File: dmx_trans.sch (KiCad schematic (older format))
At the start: 56 parts, among them IC1 SP3485EP, J1 DB9, K1 CONN_3, K2 CONN_3, P1 CONN_2, P2 CONN_5X2, P3 LCD_CONN, SW1 RESET_BTN, SW2 PROG_BTN, U1 NCP1117ST33T3G, U2 STM32F100C6, U3 ST3232CD, X1 8MHz

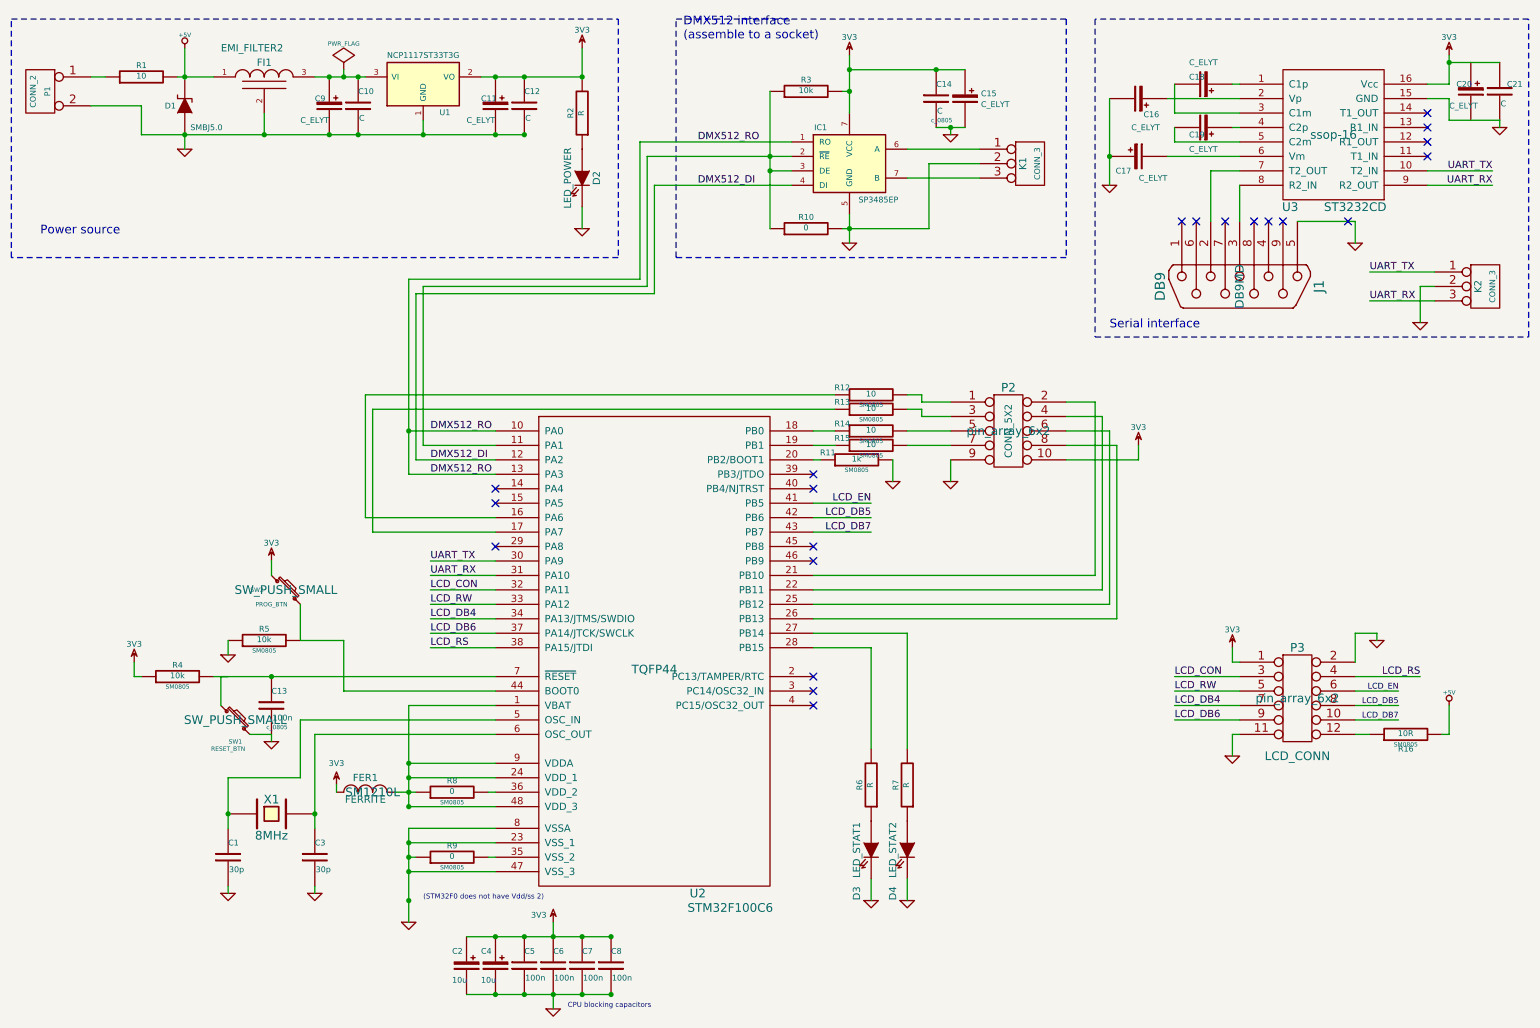
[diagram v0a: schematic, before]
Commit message: Schematics updated
- filled values
- filled title block
- connector fixes
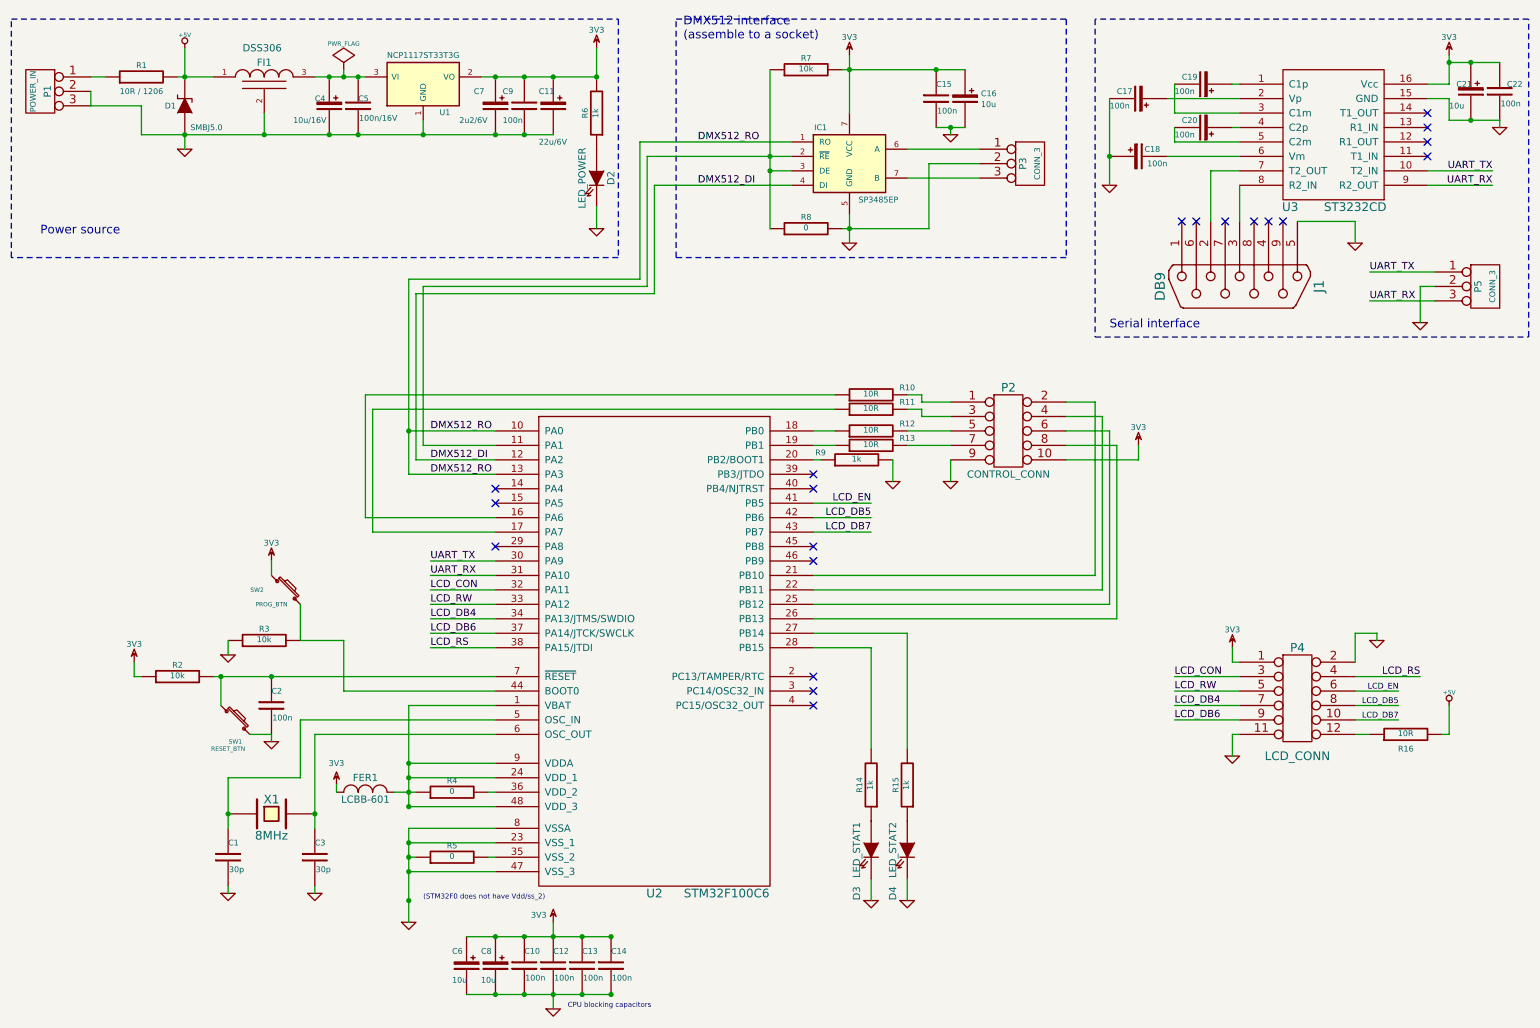
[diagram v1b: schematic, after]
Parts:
- removed P1: CONN_2, JACK_ALIM, symbol CONN_2
- added C11: 22u/6V, c_0805, symbol C_ELYT
- added P1: POWER_IN, PIN_ARRAY_3X1, symbol CONN_3
- C15: renamed from C14; value C -> 100n
- C16: renamed from C15; value C_ELYT -> 10u
- C17: renamed from C16; value C_ELYT -> 100n
- C18: renamed from C17; value C_ELYT -> 100n
- C19: renamed from C18; value C_ELYT -> 100n
- C20: renamed from C19; value C_ELYT -> 100n
- C21: renamed from C20; value C_ELYT -> 10u
- C22: renamed from C21; value C -> 100n
- C4: renamed from C9; value C_ELYT -> 10u/16V
- C5: renamed from C10; value C -> 100n/16V
- C7: renamed from C11; value C_ELYT -> 2u2/6V
- C9: renamed from C12; value C -> 100n
- FER1: value FERRITE -> LCBB-601
- FI1: value EMI_FILTER2 -> DSS306
- P2: value CONN_5X2 -> CONTROL_CONN
- R1: value 10 -> 10R / 1206
- R10: renamed from R12; value 10 -> 10R
- R11: renamed from R13; value 10 -> 10R
- R12: renamed from R14; value 10 -> 10R
- R13: renamed from R15; value 10 -> 10R
- R14: renamed from R6; value R -> 1k
- R15: renamed from R7; value R -> 1k
- R6: renamed from R2; value R -> 1k
- renumbered C5 to C10, C6 to C12, C7 to C13, C8 to C14, C13 to C2, C2 to C6, C4 to C8, K1 to P3, P3 to P4, K2 to P5, R4 to R2, R5 to R3, R8 to R4, R9 to R5, R3 to R7, R10 to R8, R11 to R9
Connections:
- net 3V3: now also C21.1, C11.1
- net GND: now also C21.2, C11.2, P1.2 (PM), P1.3 (P3)
- net at R1.1: now also P1.1 (P1)
- no-connect marks 21 -> 20
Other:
- note added: "(STM32F0 does not have Vdd/ss_2)"
- note removed: "(STM32F0 does not have Vdd/ss 2)"
- moved on the sheet: D2, R6, R7

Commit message: Start of routing
- footprints assigned
- initial part placement
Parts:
- C11, C4, C5, C6, C7, C8: footprint c_0805 -> c_tant_A
- C16, C21: footprint (none) -> c_tant_A
- C17, C18, C19, C20, C22: footprint (none) -> c_0805
- D1: footprint SM1206POL -> DO-214AA(SMB)
- FER1: footprint SM1210L -> SM0805
- FI1: footprint PIN_ARRAY_3X1 -> DSS6
- J1: footprint DB9MD -> DB9M_CI
- P1: footprint PIN_ARRAY_3X1 -> BARREL_JACK
- P2: footprint pin_array_6x2 -> PIN_ARRAY_5x2
- P3: value CONN_3 -> DMX512_CON; footprint PIN_ARRAY_3X1 -> PINHEAD1-3
- P5: value CONN_3 -> UART_CON
- R8: value 0 -> N/A
- SW1, SW2: footprint SW_PUSH_SMALL -> switch-tact-DTSM-3
- U2: footprint TQFP44 -> LQFP48
- U3: footprint ssop-16 -> SO16N
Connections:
- net +5V: now also C4.1, C5.1, FI1.3 (VO), U1.3 (VI); no longer D1.2 (K), FI1.1 (VI), R1.2
- new net: D1.2 (K), FI1.1 (VI), R1.2
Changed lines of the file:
@@
-EESchema Schematic File Version 2  date 18/05/2013 11:10:39
+EESchema Schematic File Version 2  date 18/05/2013 19:06:34
 LIBS:power
 LIBS:device
@@
 F 0 "D1" V 1850 1300 40  0000 C CNN
 F 1 "SMBJ5.0" V 1700 1050 40  0000 C CNN
-F 2 "SM1206POL" H 1850 1200 60  0001 C CNN
+F 2 "DO-214AA(SMB)" H 1850 1200 60  0001 C CNN
 F 3 "~" H 1850 1200 60  0000 C CNN
 	1    1850 1200
@@
 F 0 "FI1" H 2400 1100 50  0000 C CNN
 F 1 "DSS306" H 2250 1200 50  0000 L CNN
-F 2 "PIN_ARRAY_3X1" H 2400 1000 60  0001 C CNN
+F 2 "DSS6" H 2400 1000 60  0001 C CNN
 F 3 "~" H 2400 1000 60  0000 C CNN
 	1    2400 1000
@@
 F 0 "C5" H 3050 1250 40  0000 L CNN
 F 1 "100n/16V" H 3056 1115 40  0000 L CNN
-F 2 "c_0805" H 3088 1050 30  0001 C CNN
+F 2 "c_tant_A" H 3088 1050 30  0001 C CNN
 F 3 "~" H 3050 1200 60  0000 C CNN
 	1    3050 1200
@@
 F 0 "C4" H 2750 1250 40  0000 L CNN
 F 1 "10u/16V" H 2600 1100 40  0000 L CNN
-F 2 "c_0805" H 2888 1050 30  0001 C CNN
+F 2 "c_tant_A" H 2888 1050 30  0001 C CNN
 F 3 "~" H 2850 1200 60  0000 C CNN
 	1    2850 1200
@@
 F 0 "C7" H 3850 1300 40  0000 L CNN
 F 1 "2u2/6V" H 3750 1100 40  0000 L CNN
-F 2 "c_0805" H 4038 1050 30  0001 C CNN
+F 2 "c_tant_A" H 4038 1050 30  0001 C CNN
 F 3 "~" H 4000 1200 60  0000 C CNN
 	1    4000 1200
@@
 F 0 "C8" H 3900 7250 40  0000 L CNN
 F 1 "10u" H 3900 7050 40  0000 L CNN
-F 2 "c_0805" H 4038 7000 30  0001 C CNN
+F 2 "c_tant_A" H 4038 7000 30  0001 C CNN
 F 3 "~" H 4000 7150 60  0000 C CNN
 	1    4000 7150
@@
 F 0 "C6" H 3700 7250 40  0000 L CNN
 F 1 "10u" H 3700 7050 40  0000 L CNN
-F 2 "c_0805" H 3838 7000 30  0001 C CNN
+F 2 "c_tant_A" H 3838 7000 30  0001 C CNN
 F 3 "~" H 3800 7150 60  0000 C CNN
 	1    3800 7150
@@
 P 7700 1600
 F 0 "P3" V 7650 1600 50  0000 C CNN
-F 1 "CONN_3" V 7750 1600 40  0000 C CNN
-F 2 "PIN_ARRAY_3X1" H 7700 1600 60  0001 C CNN
+F 1 "DMX512_CON" H 7650 1400 40  0000 C CNN
+F 2 "PINHEAD1-3" H 7700 1600 60  0001 C CNN
 F 3 "" H 7700 1600 60  0000 C CNN
 	1    7700 1600
@@
 F 0 "SW1" H 2200 5300 30  0000 C CNN
 F 1 "RESET_BTN" H 2150 5250 30  0000 C CNN
-F 2 "SW_PUSH_SMALL" H 2200 5450 60  0001 C CNN
+F 2 "switch-tact-DTSM-3" H 2200 5450 60  0001 C CNN
 F 3 "~" H 2200 5450 60  0000 C CNN
 	1    2200 5450
@@
 F 0 "U2" H 5100 3550 60  0000 C CNN
 F 1 "STM32F100C6" H 5600 3550 60  0000 C CNN
-F 2 "TQFP44" H 5100 5100 60  0001 C CNN
+F 2 "LQFP48" H 5100 5100 60  0001 C CNN
 F 3 "" H 5100 5100 60  0000 C CNN
 	1    5100 5100
@@
 F 0 "SW2" H 2350 4550 30  0000 C CNN
 F 1 "PROG_BTN" H 2450 4450 30  0000 C CNN
-F 2 "SW_PUSH_SMALL" H 2550 4550 60  0001 C CNN
+F 2 "switch-tact-DTSM-3" H 2550 4550 60  0001 C CNN
 F 3 "~" H 2550 4550 60  0000 C CNN
 	1    2550 4550
@@
 P 10850 2450
 F 0 "P5" V 10800 2450 50  0000 C CNN
-F 1 "CONN_3" V 10900 2450 40  0000 C CNN
+F 1 "UART_CON" V 10900 2450 40  0000 C CNN
 F 2 "PIN_ARRAY_3X1" H 10850 2450 60  0001 C CNN
 F 3 "" H 10850 2450 60  0000 C CNN
@@
 F 0 "FER1" H 3100 6050 50  0000 C CNN
 F 1 "LCBB-601" H 3100 5900 50  0000 C CNN
-F 2 "SM1210L" H 3150 5950 60  0001 C CNN
+F 2 "SM0805" H 3150 5950 60  0001 C CNN
 F 3 "~" H 3150 5950 60  0000 C CNN
 	1    3100 5950
@@
 F 0 "C16" H 7360 1185 40  0000 L CNN
 F 1 "10u" H 7360 1110 40  0000 L CNN
-F 2 "" H 7288 1000 30  0000 C CNN
+F 2 "c_tant_A" H 7288 1000 30  0001 C CNN
 F 3 "~" H 7250 1150 60  0000 C CNN
 	1    7250 1150
@@
 F 0 "P2" H 7550 3750 60  0000 C CNN
 F 1 "CONTROL_CONN" H 7550 3150 50  0000 C CNN
-F 2 "pin_array_6x2" H 7550 3450 60  0001 C CNN
+F 2 "PIN_ARRAY_5x2" H 7550 3450 60  0001 C CNN
 F 3 "" H 7550 3450 60  0000 C CNN
 	1    7550 3450
@@
 F 0 "U3" H 9500 900 60  0000 C CNN
 F 1 "ST3232CD" H 9950 900 60  0000 C CNN
-F 2 "ssop-16" H 9800 1400 60  0001 C CNN
+F 2 "SO16N" H 9800 1400 60  0001 C CNN
 F 3 "" H 9800 1400 60  0000 C CNN
 	1    9800 1400
@@
 F 0 "C19" V 8850 900 40  0000 L CNN
 F 1 "100n" V 8950 850 40  0000 L CNN
-F 2 "" H 8938 900 30  0000 C CNN
+F 2 "c_0805" H 8938 900 30  0001 C CNN
 F 3 "~" H 8900 1050 60  0000 C CNN
 	1    8900 1050
@@
 F 0 "C17" V 8400 1000 40  0000 L CNN
 F 1 "100n" V 8500 950 40  0000 L CNN
-F 2 "" H 8488 1000 30  0000 C CNN
+F 2 "c_0805" H 8488 1000 30  0001 C CNN
 F 3 "~" H 8450 1150 60  0000 C CNN
 	1    8450 1150
@@
 F 0 "C18" V 8500 1400 40  0000 L CNN
 F 1 "100n" V 8400 1350 40  0000 L CNN
-F 2 "" H 8488 1400 30  0000 C CNN
+F 2 "c_0805" H 8488 1400 30  0001 C CNN
 F 3 "~" H 8450 1550 60  0000 C CNN
 	1    8450 1550
@@
 F 0 "C20" V 8850 1200 40  0000 L CNN
 F 1 "100n" V 8950 1150 40  0000 L CNN
-F 2 "" H 8938 1200 30  0000 C CNN
+F 2 "c_0805" H 8938 1200 30  0001 C CNN
 F 3 "~" H 8900 1350 60  0000 C CNN
 	1    8900 1350
@@
 F 0 "C22" H 11000 1150 40  0000 L CNN
 F 1 "100n" H 10956 1015 40  0000 L CNN
-F 2 "" H 10988 950 30  0000 C CNN
+F 2 "c_0805" H 10988 950 30  0001 C CNN
 F 3 "~" H 10940 1115 60  0000 C CNN
 	1    10950 1100
@@
 F 0 "C21" H 10650 1150 40  0000 L CNN
 F 1 "10u" H 10600 1000 40  0000 L CNN
-F 2 "" H 10788 950 30  0000 C CNN
+F 2 "c_tant_A" H 10788 950 30  0001 C CNN
 F 3 "~" H 10750 1100 60  0000 C CNN
 	1    10750 1100
@@
 F 0 "J1" H 9150 3000 70  0000 C CNN
 F 1 "DB9" H 9150 1900 70  0000 C CNN
-F 2 "DB9MD" H 9150 2450 60  0001 C CNN
+F 2 "DB9M_CI" H 9150 2450 60  0001 C CNN
 F 3 "" H 9150 2450 60  0000 C CNN
 	1    9150 2450
@@
 L +5V #PWR025
 U 1 1 5195386E
-P 1850 800
-F 0 "#PWR025" H 1850 890 20  0001 C CNN
-F 1 "+5V" H 1850 890 30  0000 C CNN
-F 2 "" H 1850 800 60  0000 C CNN
-F 3 "" H 1850 800 60  0000 C CNN
-	1    1850 800
-	1    0    0    -1
-$EndComp
-Wire Wire Line
-	1850 800  1850 1000
+P 2750 800
+F 0 "#PWR025" H 2750 890 20  0001 C CNN
+F 1 "+5V" H 2750 890 30  0000 C CNN
+F 2 "" H 2750 800 60  0000 C CNN
+F 3 "" H 2750 800 60  0000 C CNN
+	1    2750 800
+	1    0    0    -1
+$EndComp
+Wire Wire Line
+	2750 800  2750 1000
 $Comp
 L R R13
@@
 P 6150 2050
 F 0 "R8" V 6230 2050 40  0000 C CNN
-F 1 "0" V 6157 2051 40  0000 C CNN
+F 1 "N/A" V 6157 2051 40  0000 C CNN
 F 2 "SM0805" V 6080 2050 30  0001 C CNN
 F 3 "~" H 6150 2050 30  0000 C CNN
@@
 F 0 "C11" H 4300 1300 40  0000 L CNN
 F 1 "22u/6V" H 4300 950 40  0000 L CNN
-F 2 "c_0805" H 4438 1050 30  0001 C CNN
+F 2 "c_tant_A" H 4438 1050 30  0001 C CNN
 F 3 "~" H 4400 1200 60  0000 C CNN
 	1    4400 1200
@@
 F 0 "P1" V 800 1100 50  0000 C CNN
 F 1 "POWER_IN" V 900 1100 40  0000 C CNN
-F 2 "PIN_ARRAY_3X1" H 850 1100 60  0001 C CNN
+F 2 "BARREL_JACK" H 850 1100 60  0001 C CNN
 F 3 "" H 850 1100 60  0000 C CNN
 	1    850  1100
